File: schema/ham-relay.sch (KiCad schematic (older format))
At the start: 48 parts, among them J1 DB9, P1 JTAG, P2 CONN_01X08, P3 RESET, P4 ISP, P5 CONN_01X03, U1 REG3V3, U2 CPC1017N, U3 LPC1114FN28/102, U4 XYZ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

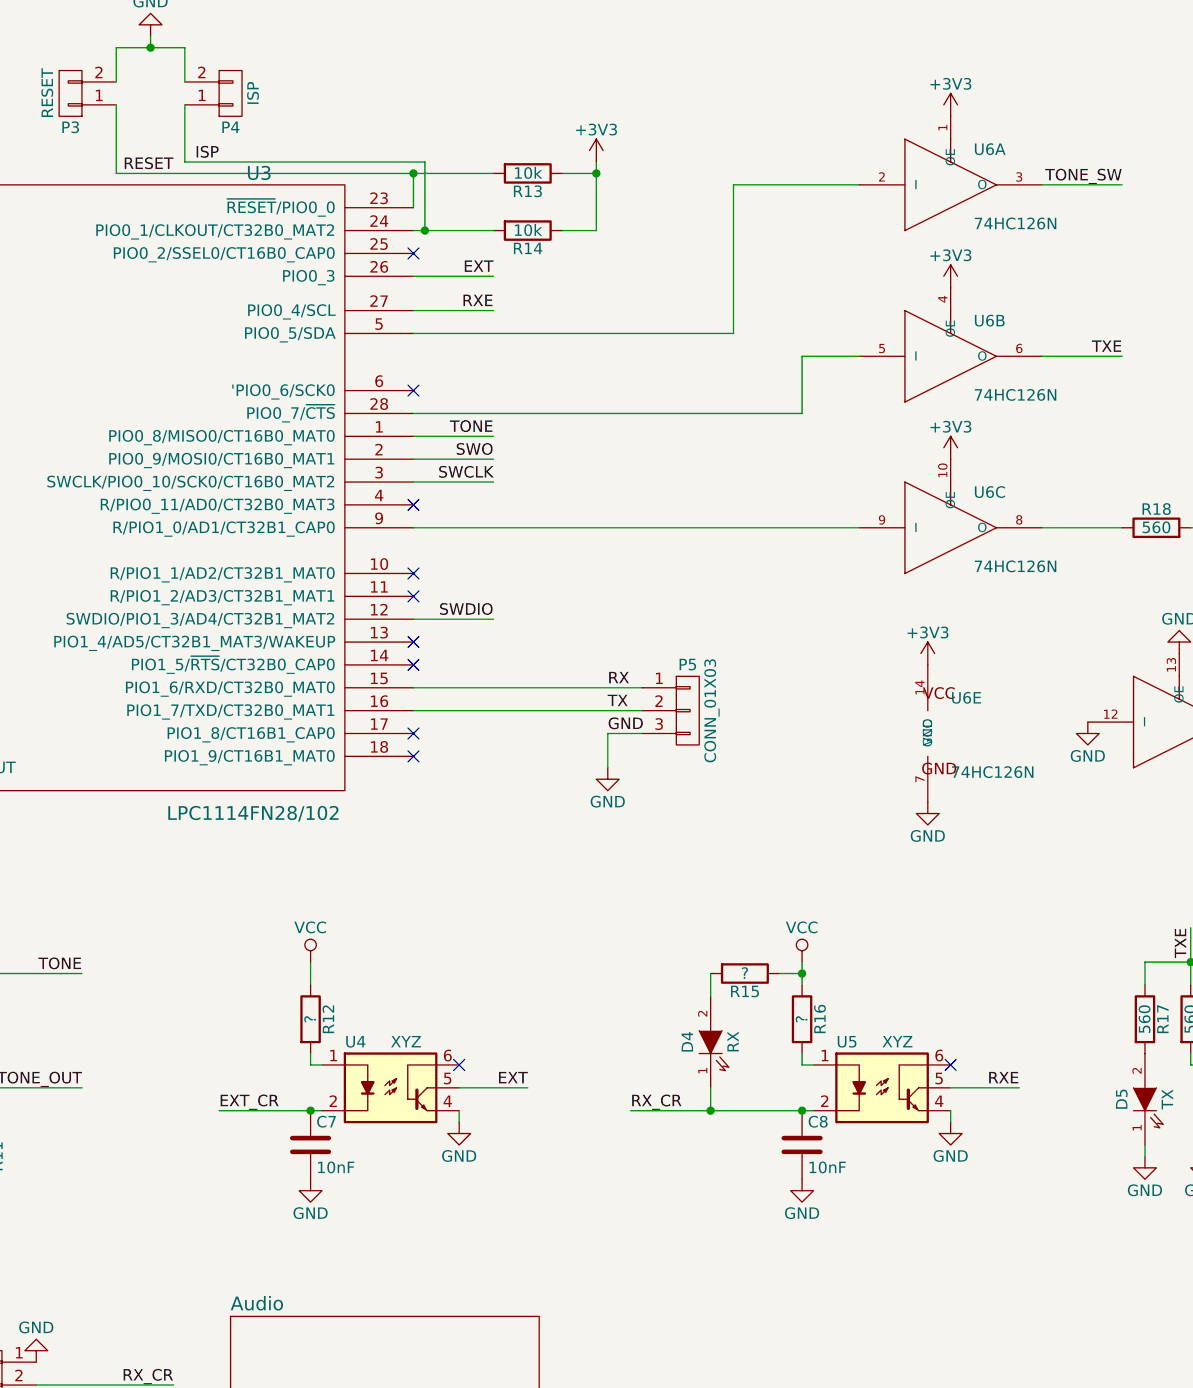
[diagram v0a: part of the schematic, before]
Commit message: * Add EXT LED * Silkscreen
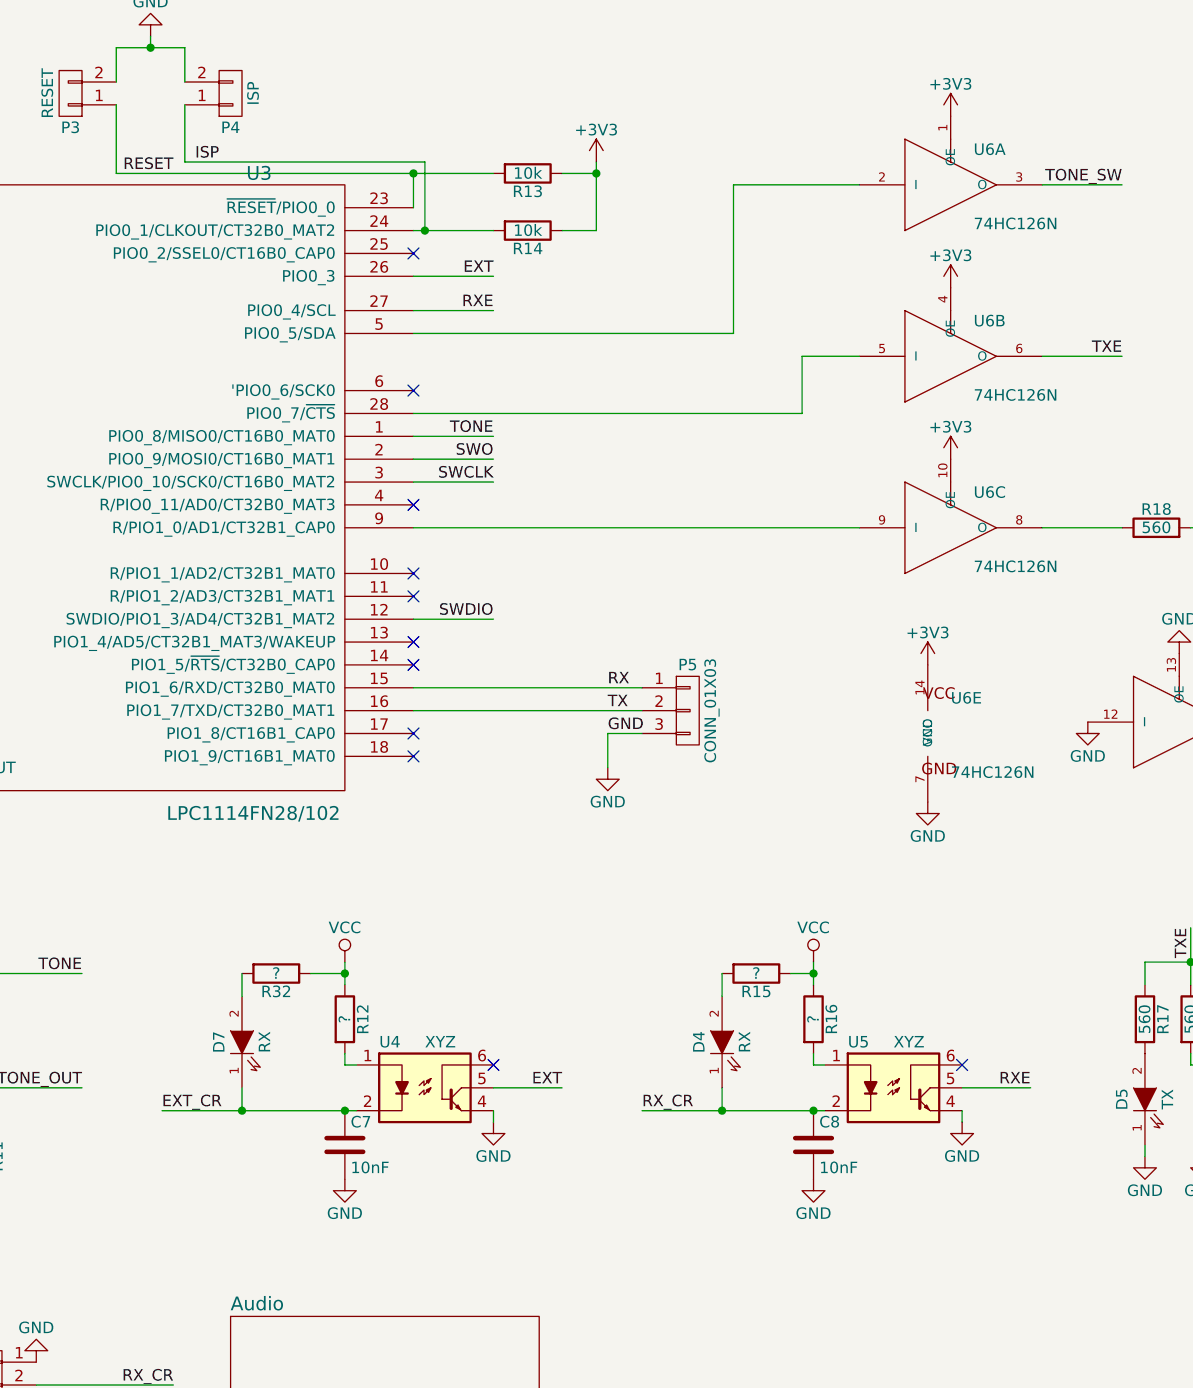
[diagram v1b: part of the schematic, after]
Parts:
- added D7: RX, LEDs:LED-3MM, symbol LED
- added R32: ?, resistors:Resistor_Horizontal_RM08mm, symbol R
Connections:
- net EXT_CR: now also D7.1 (K)
- net VCC: now also R32.1
- new net: D7.2 (A), R32.2
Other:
- moved on the sheet: C7, C8, D4, R12, R15, R16, U4, U5

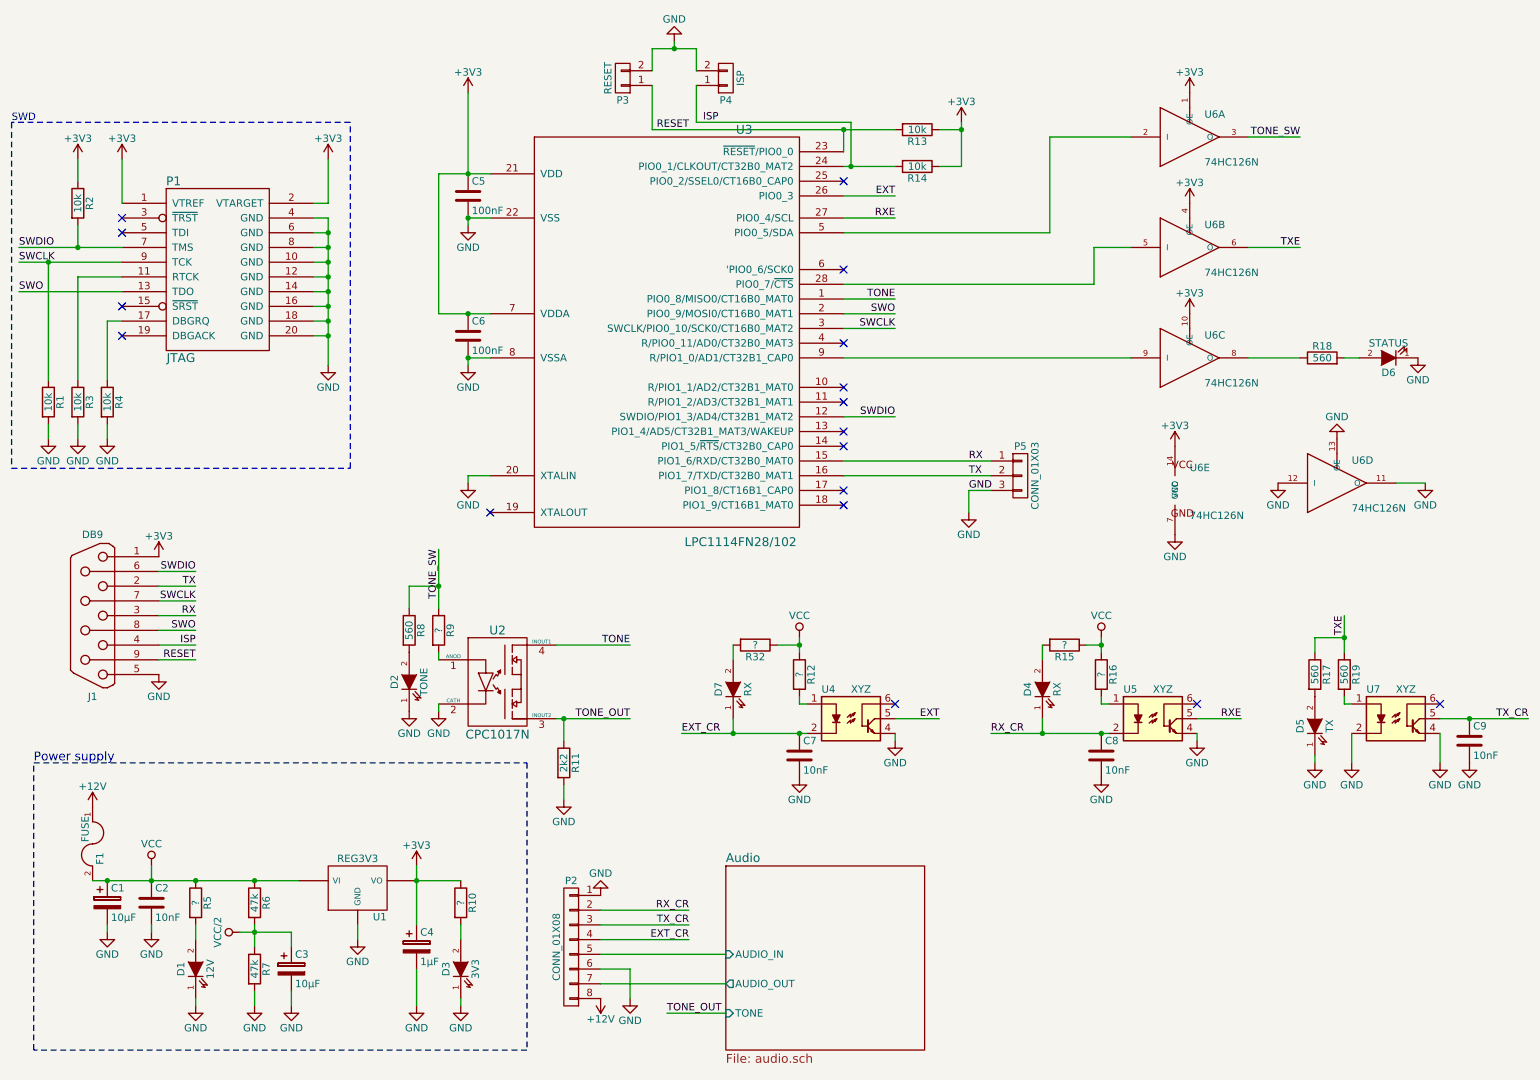
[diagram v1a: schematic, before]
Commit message: Start fixing schematics
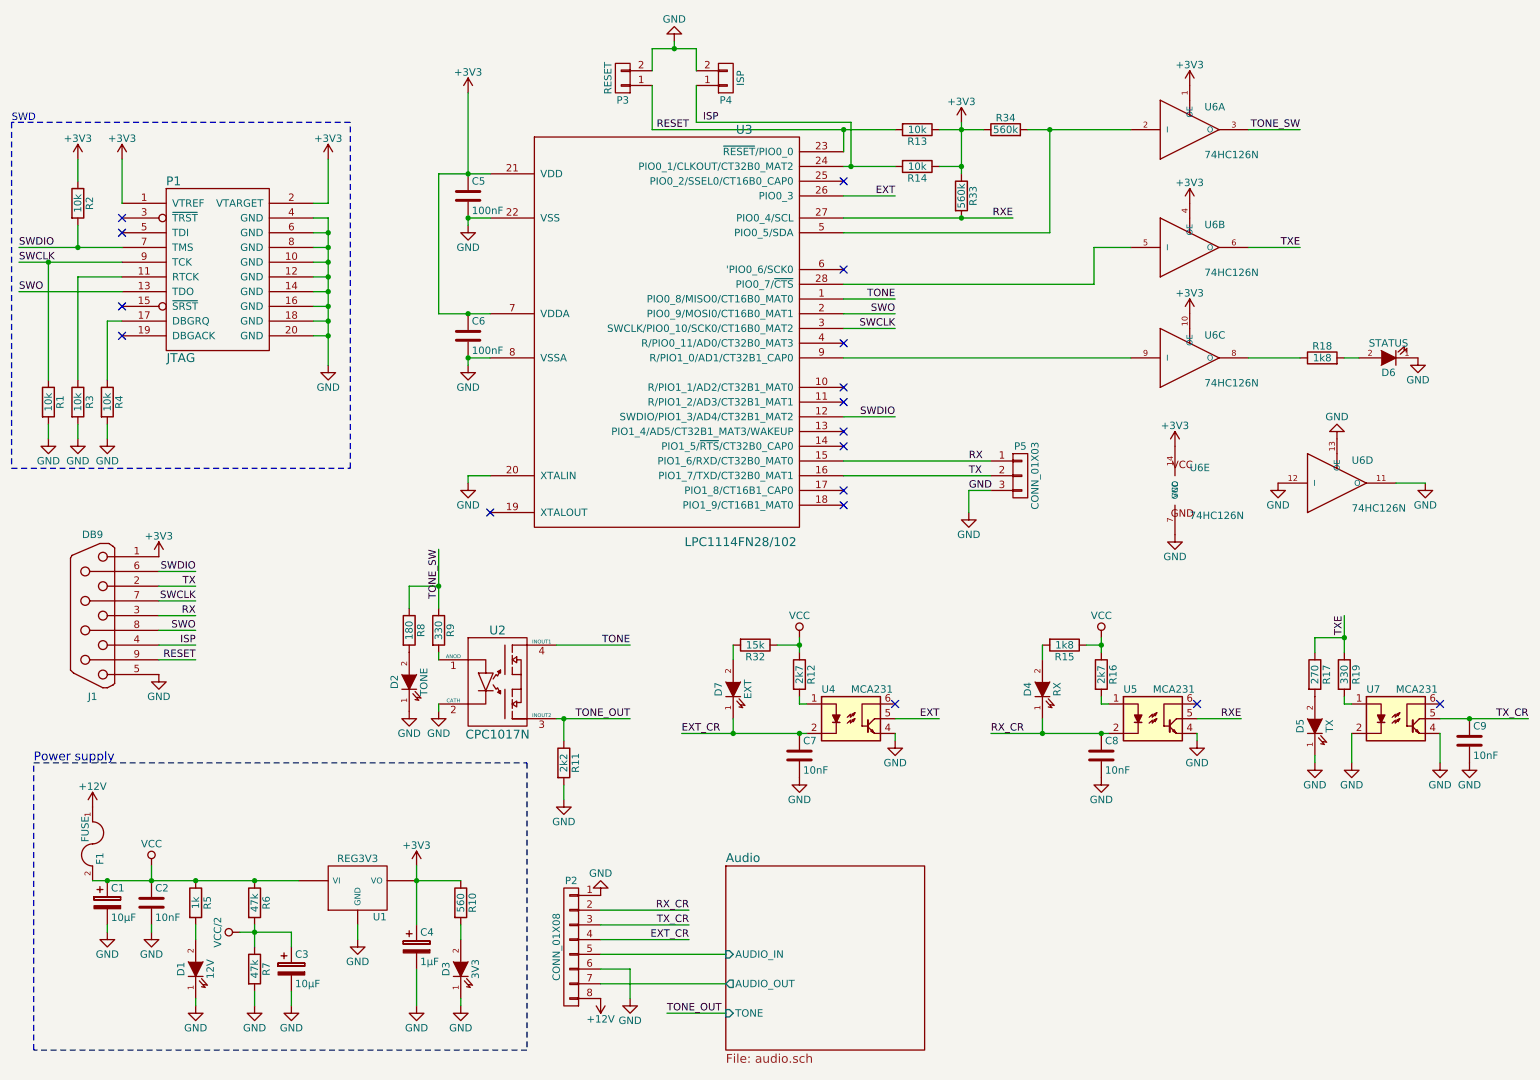
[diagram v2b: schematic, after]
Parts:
- added R33, R34: 560k, resistors:Resistor_Horizontal_RM08mm, symbol R
- D7: value RX -> EXT
- R10: value ? -> 560
- R12, R16: value ? -> 2k7
- R15: value ? -> 1k8
- R17: value 560 -> 270
- R18: value 560 -> 1k8
- R19: value 560 -> 330
- R32: value ? -> 15k
- R5: value ? -> 1k
- R8: value 560 -> 180
- R9: value ? -> 330
- U4, U5, U7: value XYZ -> MCA231
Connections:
- net +3V3: now also R33.1, R34.1
- net RXE: now also R33.2
- net at U3.5 (PIO0_5/SDA), U6.2 (I): now also R34.2
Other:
- moved on the sheet: U6A
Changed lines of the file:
@@
 Sheet 1 2
 Title "Logique relais"
-Date "2016-02-14"
-Rev "6"
+Date "2016-04-08"
+Rev "7"
 Comp ""
 Comment1 ""
@@
 	6250 2350 7950 2350
 Wire Wire Line
-	6250 2000 7650 2000
+	7650 2000 6250 2000
 $Comp
 L GND #PWR06
@@
 P 3500 4700
 F 0 "R9" V 3580 4700 50  0000 C CNN
-F 1 "?" V 3500 4700 50  0000 C CNN
+F 1 "330" V 3500 4700 50  0000 C CNN
 F 2 "resistors:Resistor_Horizontal_RM08mm" V 3430 4700 30  0001 C CNN
 F 3 "" H 3500 4700 30  0000 C CNN
@@
 P 3300 4700
 F 0 "R8" V 3380 4700 50  0000 C CNN
-F 1 "560" V 3300 4700 50  0000 C CNN
+F 1 "180" V 3300 4700 50  0000 C CNN
 F 2 "resistors:Resistor_Horizontal_RM08mm" V 3230 4700 30  0001 C CNN
 F 3 "" H 3300 4700 30  0000 C CNN
@@
 P 8350 5300
 F 0 "U5" H 8150 5500 50  0000 L CNN
-F 1 "XYZ" H 8350 5500 50  0000 L CNN
+F 1 "MCA231" H 8350 5500 50  0000 L CNN
 F 2 "Housings_DIP:DIP-6_W7.62mm" H 8350 5300 50  0001 L CNN
 F 3 "" H 8350 5300 50  0000 L CNN
@@
 P 8000 5000
 F 0 "R16" V 8080 5000 50  0000 C CNN
-F 1 "?" V 8000 5000 50  0000 C CNN
+F 1 "2k7" V 8000 5000 50  0000 C CNN
 F 2 "resistors:Resistor_Horizontal_RM08mm" V 7930 5000 30  0001 C CNN
 F 3 "" H 8000 5000 30  0000 C CNN
@@
 	8650 5300 8950 5300
 Wire Wire Line
-	6250 1900 6600 1900
-Text Label 6600 1900 2    50   ~ 0
+	6250 1900 7400 1900
+Text Label 7400 1900 2    50   ~ 0
 RXE
 Text Label 8950 5300 2    50   ~ 0
@@
 P 10000 5300
 F 0 "U7" H 9800 5500 50  0000 L CNN
-F 1 "XYZ" H 10000 5500 50  0000 L CNN
+F 1 "MCA231" H 10000 5500 50  0000 L CNN
 F 2 "Housings_DIP:DIP-6_W7.62mm" H 10000 5300 50  0001 L CNN
 F 3 "" H 10000 5300 50  0000 L CNN
@@
 P 9650 5000
 F 0 "R19" V 9730 5000 50  0000 C CNN
-F 1 "560" V 9650 5000 50  0000 C CNN
+F 1 "330" V 9650 5000 50  0000 C CNN
 F 2 "resistors:Resistor_Horizontal_RM08mm" V 9580 5000 30  0001 C CNN
 F 3 "" H 9650 5000 30  0000 C CNN
@@
 P 9450 5000
 F 0 "R17" V 9530 5000 50  0000 C CNN
-F 1 "560" V 9450 5000 50  0000 C CNN
+F 1 "270" V 9450 5000 50  0000 C CNN
 F 2 "resistors:Resistor_Horizontal_RM08mm" V 9380 5000 30  0001 C CNN
 F 3 "" H 9450 5000 30  0000 C CNN
@@
 P 7750 4800
 F 0 "R15" V 7830 4800 50  0000 C CNN
-F 1 "?" V 7750 4800 50  0000 C CNN
+F 1 "1k8" V 7750 4800 50  0000 C CNN
 F 2 "resistors:Resistor_Horizontal_RM08mm" V 7680 4800 30  0001 C CNN
 F 3 "" H 7750 4800 30  0000 C CNN
@@
 P 9500 2850
 F 0 "R18" V 9580 2850 50  0000 C CNN
-F 1 "560" V 9500 2850 50  0000 C CNN
+F 1 "1k8" V 9500 2850 50  0000 C CNN
 F 2 "resistors:Resistor_Horizontal_RM08mm" V 9430 2850 30  0001 C CNN
 F 3 "" H 9500 2850 30  0000 C CNN
@@
 	7050 1550 6900 1550
 Wire Wire Line
-	7050 1250 7050 1550
+	7050 1250 7050 1600
 Wire Wire Line
 	8200 2850 6250 2850
@@
 L 74HC126N U6
 U 1 1 567894D6
-P 8600 1350
-F 0 "U6" H 8700 1475 50  0000 L BNN
-F 1 "74HC126N" H 8700 1150 50  0000 L BNN
-F 2 "Housings_DIP:DIP-14_W7.62mm" H 8600 1500 50  0001 C CNN
-F 3 "" H 8600 1350 60  0000 C CNN
-	1    8600 1350
+P 8600 1300
+F 0 "U6" H 8700 1425 50  0000 L BNN
+F 1 "74HC126N" H 8700 1100 50  0000 L BNN
+F 2 "Housings_DIP:DIP-14_W7.62mm" H 8600 1450 50  0001 C CNN
+F 3 "" H 8600 1300 60  0000 C CNN
+	1    8600 1300
 	1    0    0    -1
 $EndComp
@@
 L +3V3 #PWR030
 U 1 1 5678A2DF
-P 8600 1050
-F 0 "#PWR030" H 8600 900 50  0001 C CNN
-F 1 "+3V3" H 8600 1190 50  0000 C CNN
-F 2 "" H 8600 1050 60  0000 C CNN
-F 3 "" H 8600 1050 60  0000 C CNN
-	1    8600 1050
+P 8600 1000
+F 0 "#PWR030" H 8600 850 50  0001 C CNN
+F 1 "+3V3" H 8600 1140 50  0000 C CNN
+F 2 "" H 8600 1000 60  0000 C CNN
+F 3 "" H 8600 1000 60  0000 C CNN
+	1    8600 1000
 	1    0    0    -1
 $EndComp
@@
 $EndComp
 Wire Wire Line
-	8200 1350 7650 1350
-Wire Wire Line
-	7650 1350 7650 2000
+	7650 1300 7650 2000
 Wire Wire Line
 	7950 2350 7950 2100
@@
 	3300 4550 3300 4400
 Wire Wire Line
-	9350 1350 9000 1350
-Text Label 9350 1350 2    50   ~ 0
+	9350 1300 9000 1300
+Text Label 9350 1300 2    50   ~ 0
 TONE_SW
 Wire Wire Line
@@
 P 1850 6550
 F 0 "R5" V 1930 6550 50  0000 C CNN
-F 1 "?" V 1850 6550 50  0000 C CNN
+F 1 "1k" V 1850 6550 50  0000 C CNN
 F 2 "resistors:Resistor_Horizontal_RM08mm" V 1780 6550 30  0001 C CNN
 F 3 "" H 1850 6550 30  0000 C CNN
@@
 P 3650 6550
 F 0 "R10" V 3730 6550 50  0000 C CNN
-F 1 "?" V 3650 6550 50  0000 C CNN
+F 1 "560" V 3650 6550 50  0000 C CNN
 F 2 "resistors:Resistor_Horizontal_RM08mm" V 3580 6550 30  0001 C CNN
 F 3 "" H 3650 6550 30  0000 C CNN
@@
 Connection ~ 6250 1300
 Wire Wire Line
-	6900 1300 7050 1300
+	6900 1300 7200 1300
 Connection ~ 7050 1300
 Wire Wire Line
@@
 P 6300 5300
 F 0 "U4" H 6100 5500 50  0000 L CNN
-F 1 "XYZ" H 6300 5500 50  0000 L CNN
+F 1 "MCA231" H 6300 5500 50  0000 L CNN
 F 2 "Housings_DIP:DIP-6_W7.62mm" H 6300 5300 50  0001 L CNN
 F 3 "" H 6300 5300 50  0000 L CNN
@@
 P 5950 5000
 F 0 "R12" V 6030 5000 50  0000 C CNN
-F 1 "?" V 5950 5000 50  0000 C CNN
+F 1 "2k7" V 5950 5000 50  0000 C CNN
 F 2 "resistors:Resistor_Horizontal_RM08mm" V 5880 5000 30  0001 C CNN
 F 3 "" H 5950 5000 30  0000 C CNN
@@
 P 5650 4800
 F 0 "R32" V 5730 4800 50  0000 C CNN
-F 1 "?" V 5650 4800 50  0000 C CNN
+F 1 "15k" V 5650 4800 50  0000 C CNN
 F 2 "resistors:Resistor_Horizontal_RM08mm" V 5580 4800 30  0001 C CNN
 F 3 "" H 5650 4800 30  0000 C CNN
@@
 P 5500 5100
 F 0 "D7" H 5500 5200 50  0000 C CNN
-F 1 "RX" H 5500 5000 50  0000 C CNN
+F 1 "EXT" H 5500 5000 50  0000 C CNN
 F 2 "LEDs:LED-3MM" H 5500 5100 60  0001 C CNN
 F 3 "" H 5500 5100 60  0000 C CNN
@@
 Text Label 5150 5400 0    50   ~ 0
 EXT_CR
+$Comp
+L R R34
+U 1 1 57083520
+P 7350 1300
+F 0 "R34" V 7430 1300 50  0000 C CNN
+F 1 "560k" V 7350 1300 50  0000 C CNN
+F 2 "resistors:Resistor_Horizontal_RM08mm" V 7280 1300 30  0001 C CNN
+F 3 "" H 7350 1300 30  0000 C CNN
+	1    7350 1300
+	0    -1   -1   0
+$EndComp
+Wire Wire Line
+	7500 1300 8200 1300
+$Comp
+L R R33
+U 1 1 570838EB
+P 7050 1750
+F 0 "R33" V 7130 1750 50  0000 C CNN
+F 1 "560k" V 7050 1750 50  0000 C CNN
+F 2 "resistors:Resistor_Horizontal_RM08mm" V 6980 1750 30  0001 C CNN
+F 3 "" H 7050 1750 30  0000 C CNN
+	1    7050 1750
+	1    0    0    -1
+$EndComp
+Connection ~ 7050 1550
+Connection ~ 7050 1900
+Connection ~ 7650 1300
 $EndSCHEMATC
